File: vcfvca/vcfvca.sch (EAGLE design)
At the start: 104 parts, among them IC1 LM13700N, IC2 LM4558N, IC3 LM13700N, IC4 LM13700N, IC5 LM4558N, J1 POWER, J2 FREQ, J3 RES, J4 AMP, J5 AUD_IN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

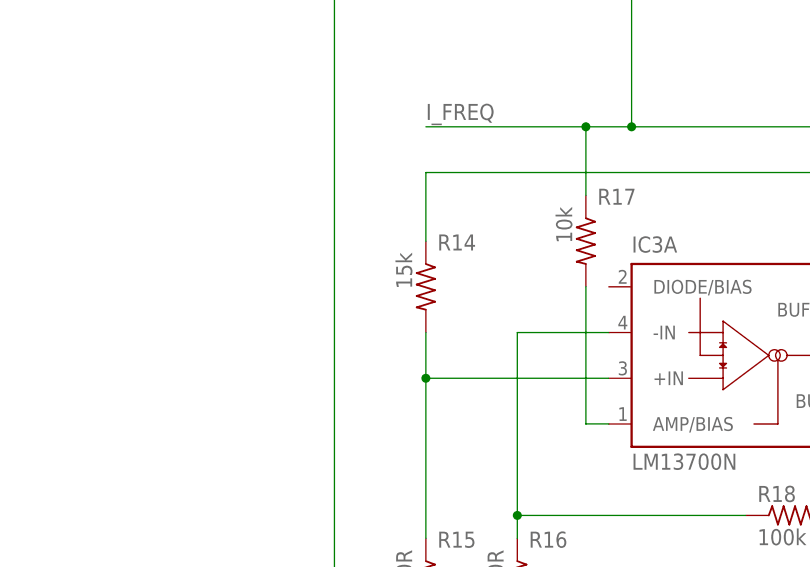
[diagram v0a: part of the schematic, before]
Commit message: Fix component value. Export to image
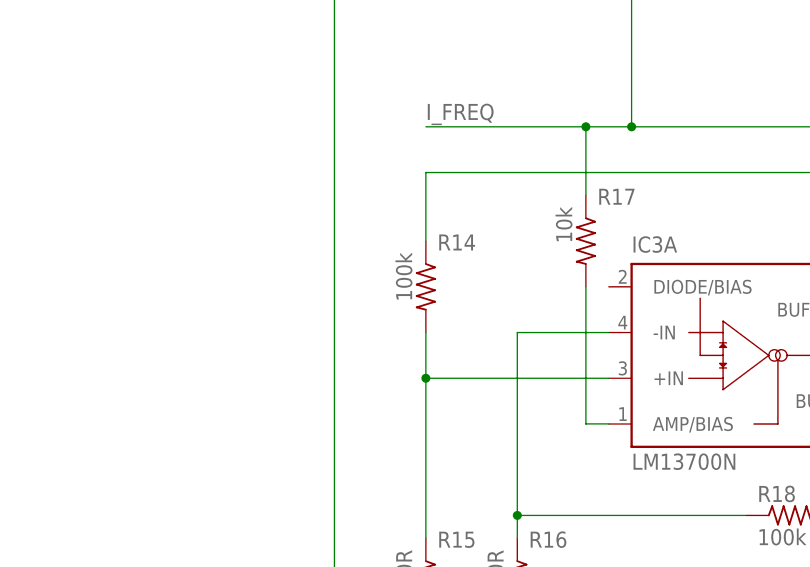
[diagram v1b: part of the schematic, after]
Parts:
- R14: value 15k -> 100k
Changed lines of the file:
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@@
 <part name="R18" library="rcl" library_urn="urn:adsk.eagle:library:334" deviceset="R-US_" device="0207/10" package3d_urn="urn:adsk.eagle:package:23491/2" value="100k"/>
 <part name="R19" library="rcl" library_urn="urn:adsk.eagle:library:334" deviceset="R-US_" device="0207/10" package3d_urn="urn:adsk.eagle:package:23491/2" value="15k"/>
-<part name="R14" library="rcl" library_urn="urn:adsk.eagle:library:334" deviceset="R-US_" device="0207/10" package3d_urn="urn:adsk.eagle:package:23491/2" value="15k"/>
+<part name="R14" library="rcl" library_urn="urn:adsk.eagle:library:334" deviceset="R-US_" device="0207/10" package3d_urn="urn:adsk.eagle:package:23491/2" value="100k"/>
 <part name="SUPPLY8" library="supply2" library_urn="urn:adsk.eagle:library:372" deviceset="+15V" device=""/>
 <part name="GND10" library="supply1" library_urn="urn:adsk.eagle:library:371" deviceset="GND" device=""/>

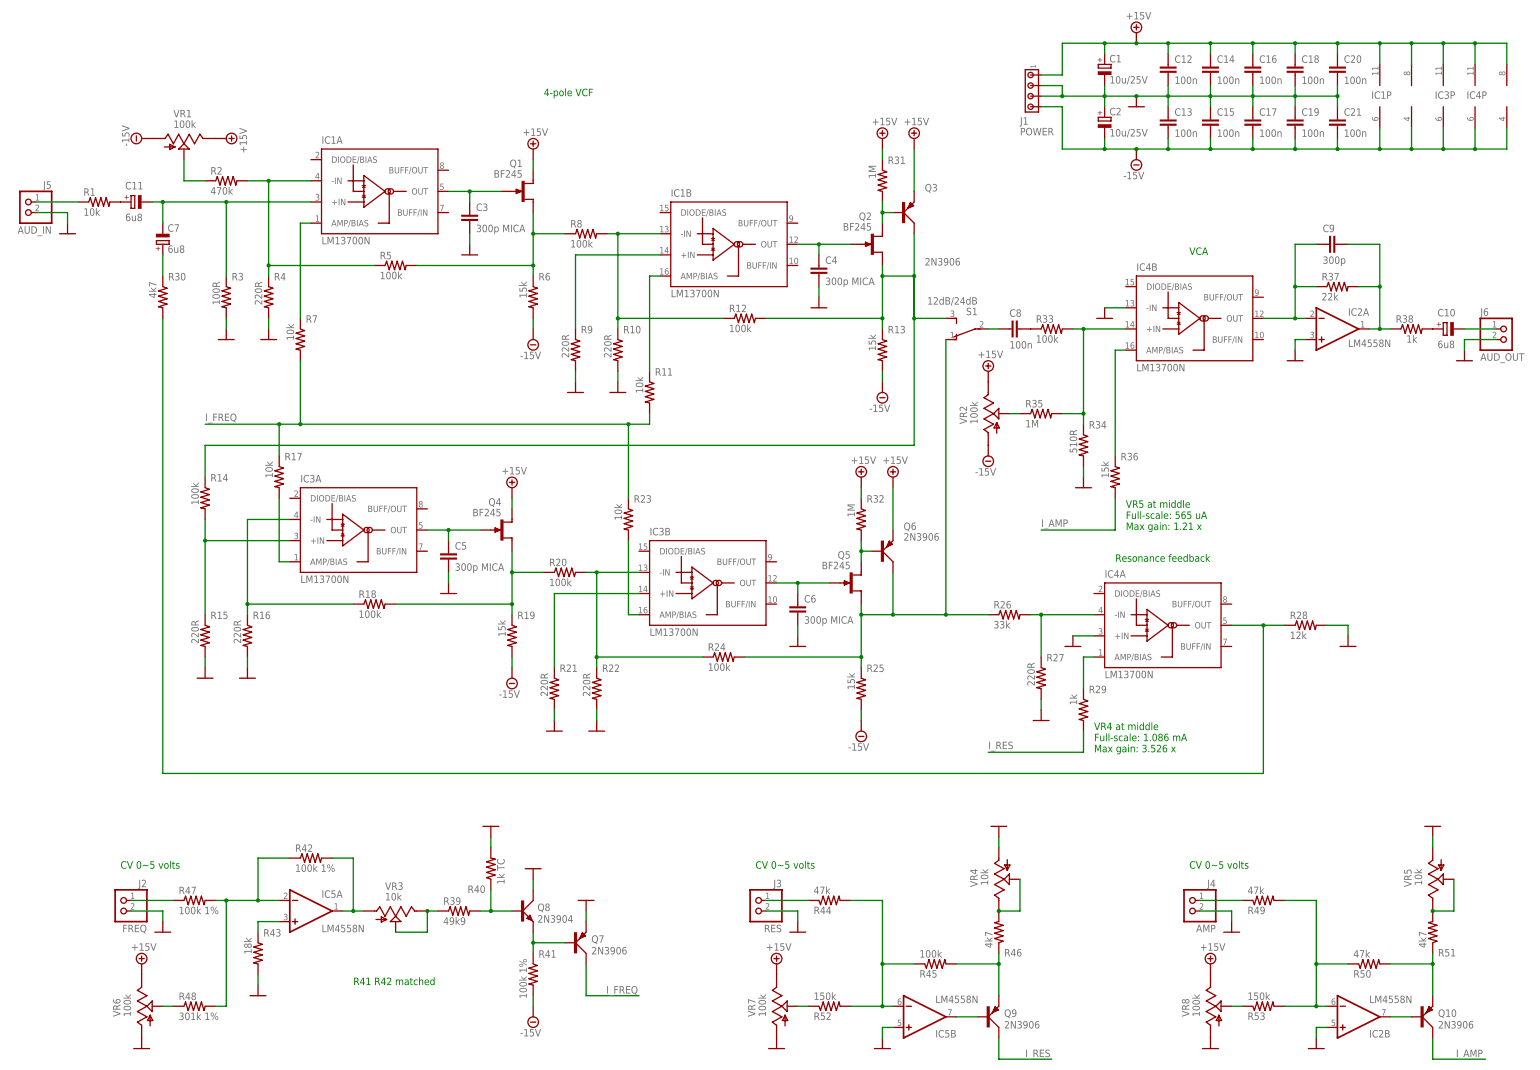
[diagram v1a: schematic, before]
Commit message: Start board placement
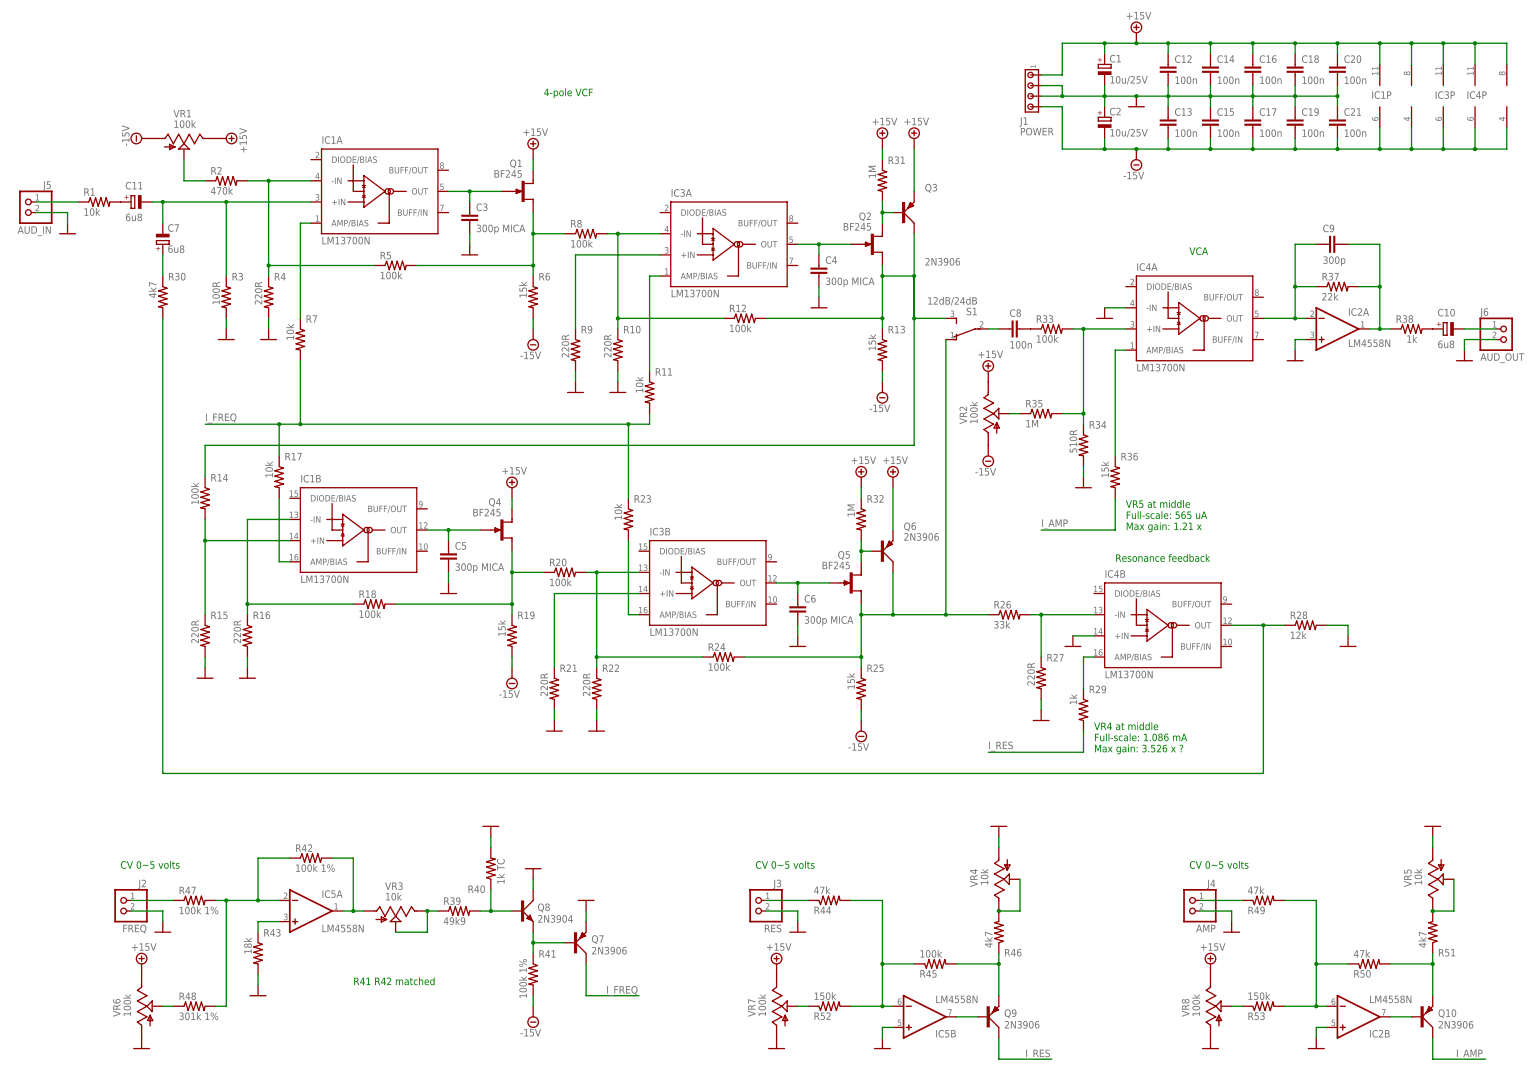
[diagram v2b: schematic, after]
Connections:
- net GND: now also IC4A.-IN, IC4B.+IN; no longer IC4A.+IN, IC4B.-IN
- net N$10: now also IC3A.AMP/BIAS; no longer IC1B.AMP/BIAS
- net N$11: now also IC3A.+IN; no longer IC1B.+IN
- net N$12: now also IC3A.-IN; no longer IC1B.-IN
- net N$14: now also IC1B.+IN; no longer IC3A.+IN
- net N$15: now also IC1B.-IN; no longer IC3A.-IN
- net N$16: now also IC4B.-IN; no longer IC4A.-IN
- net N$2: now also IC3A.OUT; no longer IC1B.OUT
- net N$22: now also IC4B.AMP/BIAS; no longer IC4A.AMP/BIAS
- net N$23: now also IC1B.AMP/BIAS; no longer IC3A.AMP/BIAS
- net N$25: now also IC4B.OUT; no longer IC4A.OUT
- net N$30: now also IC4A.+IN; no longer IC4B.+IN
- net N$31: now also IC4A.OUT; no longer IC4B.OUT
- net N$33: now also IC4A.AMP/BIAS; no longer IC4B.AMP/BIAS
- net N$4: now also IC1B.OUT; no longer IC3A.OUT
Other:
- note added: "VR4 at middle Full-scale: 1.086 mA Max gain: 3.526 x ?"
- note removed: "VR4 at middle Full-scale: 1.086 mA Max gain: 3.526 x"
- moved on the sheet: IC1B, IC3A, IC4A, IC4B
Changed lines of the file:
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@@
 <text x="261.62" y="78.74" size="1.778" layer="91">VR4 at middle
 Full-scale: 1.086 mA
-Max gain: 3.526 x</text>
+Max gain: 3.526 x ?</text>
 <text x="129.54" y="236.22" size="1.778" layer="91">4-pole VCF</text>
 <text x="284.48" y="198.12" size="1.778" layer="91">VCA</text>
@@
 <attribute name="NAME" x="328.168" y="235.585" size="1.778" layer="95"/>
 </instance>
-<instance part="IC1" gate="B" x="172.72" y="200.66" smashed="yes">
+<instance part="IC3" gate="A" x="172.72" y="200.66" smashed="yes">
 <attribute name="NAME" x="160.02" y="212.09" size="1.778" layer="95"/>
 <attribute name="VALUE" x="160.02" y="187.96" size="1.778" layer="96"/>
@@
 </instance>
 <instance part="IC2" gate="P" x="337.82" y="236.22" smashed="yes"/>
-<instance part="IC3" gate="A" x="83.82" y="132.08" smashed="yes">
+<instance part="IC1" gate="B" x="83.82" y="132.08" smashed="yes">
 <attribute name="NAME" x="71.12" y="143.51" size="1.778" layer="95"/>
 <attribute name="VALUE" x="71.12" y="119.38" size="1.778" layer="96"/>
@@
 <attribute name="VALUE" x="233.68" y="187.96" size="1.778" layer="96" rot="R180"/>
 </instance>
-<instance part="IC4" gate="B" x="284.48" y="182.88" smashed="yes">
+<instance part="IC4" gate="A" x="284.48" y="182.88" smashed="yes">
 <attribute name="NAME" x="271.78" y="194.31" size="1.778" layer="95"/>
 <attribute name="VALUE" x="271.78" y="170.18" size="1.778" layer="96"/>
@@
 <attribute name="NAME" x="351.028" y="235.585" size="1.778" layer="95"/>
 </instance>
-<instance part="IC4" gate="A" x="276.86" y="109.22" smashed="yes">
+<instance part="IC4" gate="B" x="276.86" y="109.22" smashed="yes">
 <attribute name="NAME" x="264.16" y="120.65" size="1.778" layer="95"/>
 <attribute name="VALUE" x="264.16" y="96.52" size="1.778" layer="96"/>
@@
 </segment>
 <segment>
-<pinref part="IC4" gate="A" pin="+IN"/>
+<pinref part="IC4" gate="B" pin="+IN"/>
 <pinref part="GND16" gate="1" pin="GND"/>
 <wire x1="261.62" y1="106.68" x2="256.54" y2="106.68" width="0.1524" layer="91"/>
@@
 <segment>
 <pinref part="GND18" gate="1" pin="GND"/>
-<pinref part="IC4" gate="B" pin="-IN"/>
+<pinref part="IC4" gate="A" pin="-IN"/>
 <wire x1="264.16" y1="185.42" x2="269.24" y2="185.42" width="0.1524" layer="91"/>
 </segment>
@@
 <net name="N$2" class="0">
 <segment>
-<pinref part="IC1" gate="B" pin="OUT"/>
+<pinref part="IC3" gate="A" pin="OUT"/>
 <pinref part="Q2" gate="1" pin="G"/>
 <wire x1="190.5" y1="200.66" x2="195.58" y2="200.66" width="0.1524" layer="91"/>
@@
 <net name="N$4" class="0">
 <segment>
-<pinref part="IC3" gate="A" pin="OUT"/>
+<pinref part="IC1" gate="B" pin="OUT"/>
 <pinref part="Q4" gate="1" pin="G"/>
 <wire x1="101.6" y1="132.08" x2="106.68" y2="132.08" width="0.1524" layer="91"/>
@@
 <pinref part="R11" gate="G$1" pin="1"/>
 <wire x1="154.94" y1="170.18" x2="154.94" y2="193.04" width="0.1524" layer="91"/>
-<pinref part="IC1" gate="B" pin="AMP/BIAS"/>
+<pinref part="IC3" gate="A" pin="AMP/BIAS"/>
 <wire x1="154.94" y1="193.04" x2="157.48" y2="193.04" width="0.1524" layer="91"/>
 </segment>
@@
 <segment>
 <pinref part="R8" gate="G$1" pin="2"/>
-<pinref part="IC1" gate="B" pin="-IN"/>
+<pinref part="IC3" gate="A" pin="-IN"/>
 <wire x1="144.78" y1="203.2" x2="147.32" y2="203.2" width="0.1524" layer="91"/>
 <pinref part="R10" gate="G$1" pin="1"/>
@@
 <net name="N$11" class="0">
 <segment>
-<pinref part="IC1" gate="B" pin="+IN"/>
+<pinref part="IC3" gate="A" pin="+IN"/>
 <wire x1="157.48" y1="198.12" x2="137.16" y2="198.12" width="0.1524" layer="91"/>
 <pinref part="R9" gate="G$1" pin="1"/>
@@
 <net name="N$14" class="0">
 <segment>
-<pinref part="IC3" gate="A" pin="+IN"/>
+<pinref part="IC1" gate="B" pin="+IN"/>
 <wire x1="68.58" y1="129.54" x2="48.26" y2="129.54" width="0.1524" layer="91"/>
 <pinref part="R15" gate="G$1" pin="1"/>
@@
 <pinref part="R16" gate="G$1" pin="1"/>
 <wire x1="58.42" y1="111.76" x2="58.42" y2="114.3" width="0.1524" layer="91"/>
-<pinref part="IC3" gate="A" pin="-IN"/>
+<pinref part="IC1" gate="B" pin="-IN"/>
 <wire x1="58.42" y1="114.3" x2="58.42" y2="134.62" width="0.1524" layer="91"/>
 <wire x1="58.42" y1="134.62" x2="68.58" y2="134.62" width="0.1524" layer="91"/>
@@
 <segment>
 <pinref part="R17" gate="G$1" pin="2"/>
-<pinref part="IC3" gate="A" pin="AMP/BIAS"/>
+<pinref part="IC1" gate="B" pin="AMP/BIAS"/>
 <wire x1="68.58" y1="124.46" x2="66.04" y2="124.46" width="0.1524" layer="91"/>
 <wire x1="66.04" y1="139.7" x2="66.04" y2="124.46" width="0.1524" layer="91"/>
@@
 <net name="N$16" class="0">
 <segment>
-<pinref part="IC4" gate="A" pin="-IN"/>
+<pinref part="IC4" gate="B" pin="-IN"/>
 <pinref part="R26" gate="G$1" pin="2"/>
 <wire x1="261.62" y1="111.76" x2="248.92" y2="111.76" width="0.1524" layer="91"/>
@@
 <net name="N$22" class="0">
 <segment>
-<pinref part="IC4" gate="A" pin="AMP/BIAS"/>
+<pinref part="IC4" gate="B" pin="AMP/BIAS"/>
 <wire x1="261.62" y1="101.6" x2="259.08" y2="101.6" width="0.1524" layer="91"/>
 <pinref part="R29" gate="G$1" pin="1"/>
@@
 <net name="N$25" class="0">
 <segment>
-<pinref part="IC4" gate="A" pin="OUT"/>
+<pinref part="IC4" gate="B" pin="OUT"/>
 <wire x1="294.64" y1="109.22" x2="302.26" y2="109.22" width="0.1524" layer="91"/>
 <wire x1="302.26" y1="109.22" x2="302.26" y2="73.66" width="0.1524" layer="91"/>
@@
 <net name="N$30" class="0">
 <segment>
-<pinref part="IC4" gate="B" pin="+IN"/>
+<pinref part="IC4" gate="A" pin="+IN"/>
 <pinref part="R33" gate="G$1" pin="2"/>
 <wire x1="269.24" y1="180.34" x2="259.08" y2="180.34" width="0.1524" layer="91"/>
@@
 <net name="N$33" class="0">
 <segment>
-<pinref part="IC4" gate="B" pin="AMP/BIAS"/>
+<pinref part="IC4" gate="A" pin="AMP/BIAS"/>
 <wire x1="269.24" y1="175.26" x2="266.7" y2="175.26" width="0.1524" layer="91"/>
 <pinref part="R36" gate="G$1" pin="1"/>
@@
 <net name="N$31" class="0">
 <segment>
-<pinref part="IC4" gate="B" pin="OUT"/>
+<pinref part="IC4" gate="A" pin="OUT"/>
 <wire x1="309.88" y1="182.88" x2="302.26" y2="182.88" width="0.1524" layer="91"/>
 <pinref part="IC2" gate="A" pin="-IN"/>

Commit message: Done placement
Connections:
- net GND: now also IC4A.+IN, IC4B.-IN; no longer IC4A.-IN, IC4B.+IN
- net N$16: now also IC4A.-IN; no longer IC4B.-IN
- net N$22: now also IC4A.AMP/BIAS; no longer IC4B.AMP/BIAS
- net N$25: now also IC4A.OUT; no longer IC4B.OUT
- net N$30: now also IC4B.+IN; no longer IC4A.+IN
- net N$31: now also IC2B.-IN, IC4B.OUT; no longer IC2A.-IN, IC4A.OUT
- net N$33: now also IC4B.AMP/BIAS; no longer IC4A.AMP/BIAS
- net N$35: now also IC2B.OUT; no longer IC2A.OUT
- net N$50: now also IC2A.OUT; no longer IC2B.OUT
- net N$52: now also IC2A.-IN; no longer IC2B.-IN
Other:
- moved on the sheet: IC2A, IC2B, IC4A, IC4B
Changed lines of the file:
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@@
 <attribute name="VALUE" x="220.98" y="195.58" size="1.778" layer="96"/>
 </instance>
-<instance part="IC2" gate="A" x="320.04" y="180.34" smashed="yes" rot="MR180">
+<instance part="IC2" gate="B" x="320.04" y="180.34" smashed="yes" rot="MR180">
 <attribute name="NAME" x="322.58" y="183.515" size="1.778" layer="95"/>
 <attribute name="VALUE" x="322.58" y="176.022" size="1.778" layer="96"/>
 </instance>
-<instance part="IC2" gate="B" x="325.12" y="15.24" smashed="yes" rot="MR180">
+<instance part="IC2" gate="A" x="325.12" y="15.24" smashed="yes" rot="MR180">
 <attribute name="NAME" x="327.66" y="12.065" size="1.778" layer="95" rot="MR180"/>
 <attribute name="VALUE" x="327.66" y="20.32" size="1.778" layer="96" rot="MR180"/>
@@
 <attribute name="VALUE" x="233.68" y="187.96" size="1.778" layer="96" rot="R180"/>
 </instance>
-<instance part="IC4" gate="A" x="284.48" y="182.88" smashed="yes">
+<instance part="IC4" gate="B" x="284.48" y="182.88" smashed="yes">
 <attribute name="NAME" x="271.78" y="194.31" size="1.778" layer="95"/>
 <attribute name="VALUE" x="271.78" y="170.18" size="1.778" layer="96"/>
@@
 <attribute name="NAME" x="351.028" y="235.585" size="1.778" layer="95"/>
 </instance>
-<instance part="IC4" gate="B" x="276.86" y="109.22" smashed="yes">
+<instance part="IC4" gate="A" x="276.86" y="109.22" smashed="yes">
 <attribute name="NAME" x="264.16" y="120.65" size="1.778" layer="95"/>
 <attribute name="VALUE" x="264.16" y="96.52" size="1.778" layer="96"/>
@@
 </segment>
 <segment>
-<pinref part="IC4" gate="B" pin="+IN"/>
+<pinref part="IC4" gate="A" pin="+IN"/>
 <pinref part="GND16" gate="1" pin="GND"/>
 <wire x1="261.62" y1="106.68" x2="256.54" y2="106.68" width="0.1524" layer="91"/>
@@
 <segment>
 <pinref part="GND18" gate="1" pin="GND"/>
-<pinref part="IC4" gate="A" pin="-IN"/>
+<pinref part="IC4" gate="B" pin="-IN"/>
 <wire x1="264.16" y1="185.42" x2="269.24" y2="185.42" width="0.1524" layer="91"/>
 </segment>
 <segment>
-<pinref part="IC2" gate="A" pin="+IN"/>
+<pinref part="IC2" gate="B" pin="+IN"/>
 <pinref part="GND19" gate="1" pin="GND"/>
 <wire x1="312.42" y1="177.8" x2="309.88" y2="177.8" width="0.1524" layer="91"/>
@@
 </segment>
 <segment>
-<pinref part="IC2" gate="B" pin="+IN"/>
+<pinref part="IC2" gate="A" pin="+IN"/>
 <wire x1="317.5" y1="12.7" x2="314.96" y2="12.7" width="0.1524" layer="91"/>
 <pinref part="GND27" gate="1" pin="GND"/>
@@
 <net name="N$16" class="0">
 <segment>
-<pinref part="IC4" gate="B" pin="-IN"/>
+<pinref part="IC4" gate="A" pin="-IN"/>
 <pinref part="R26" gate="G$1" pin="2"/>
 <wire x1="261.62" y1="111.76" x2="248.92" y2="111.76" width="0.1524" layer="91"/>
@@
 <net name="N$22" class="0">
 <segment>
-<pinref part="IC4" gate="B" pin="AMP/BIAS"/>
+<pinref part="IC4" gate="A" pin="AMP/BIAS"/>
 <wire x1="261.62" y1="101.6" x2="259.08" y2="101.6" width="0.1524" layer="91"/>
 <pinref part="R29" gate="G$1" pin="1"/>
@@
 <net name="N$25" class="0">
 <segment>
-<pinref part="IC4" gate="B" pin="OUT"/>
+<pinref part="IC4" gate="A" pin="OUT"/>
 <wire x1="294.64" y1="109.22" x2="302.26" y2="109.22" width="0.1524" layer="91"/>
 <wire x1="302.26" y1="109.22" x2="302.26" y2="73.66" width="0.1524" layer="91"/>
@@
 <net name="N$30" class="0">
 <segment>
-<pinref part="IC4" gate="A" pin="+IN"/>
+<pinref part="IC4" gate="B" pin="+IN"/>
 <pinref part="R33" gate="G$1" pin="2"/>
 <wire x1="269.24" y1="180.34" x2="259.08" y2="180.34" width="0.1524" layer="91"/>
@@
 <net name="N$33" class="0">
 <segment>
-<pinref part="IC4" gate="A" pin="AMP/BIAS"/>
+<pinref part="IC4" gate="B" pin="AMP/BIAS"/>
 <wire x1="269.24" y1="175.26" x2="266.7" y2="175.26" width="0.1524" layer="91"/>
 <pinref part="R36" gate="G$1" pin="1"/>
@@
 <wire x1="325.12" y1="190.5" x2="330.2" y2="190.5" width="0.1524" layer="91"/>
 <junction x="330.2" y="190.5"/>
-<pinref part="IC2" gate="A" pin="OUT"/>
+<pinref part="IC2" gate="B" pin="OUT"/>
 <wire x1="327.66" y1="180.34" x2="330.2" y2="180.34" width="0.1524" layer="91"/>
 <junction x="330.2" y="180.34"/>
@@
 <segment>
 <pinref part="Q10" gate="1" pin="B"/>
-<pinref part="IC2" gate="B" pin="OUT"/>
+<pinref part="IC2" gate="A" pin="OUT"/>
 <wire x1="337.82" y1="15.24" x2="332.74" y2="15.24" width="0.1524" layer="91"/>
 </segment>
@@
 <net name="N$52" class="0">
 <segment>
-<pinref part="IC2" gate="B" pin="-IN"/>
+<pinref part="IC2" gate="A" pin="-IN"/>
 <pinref part="R50" gate="G$1" pin="1"/>
 <wire x1="314.96" y1="17.78" x2="317.5" y2="17.78" width="0.1524" layer="91"/>
@@
 <net name="N$31" class="0">
 <segment>
-<pinref part="IC4" gate="A" pin="OUT"/>
+<pinref part="IC4" gate="B" pin="OUT"/>
 <wire x1="309.88" y1="182.88" x2="302.26" y2="182.88" width="0.1524" layer="91"/>
-<pinref part="IC2" gate="A" pin="-IN"/>
+<pinref part="IC2" gate="B" pin="-IN"/>
 <wire x1="309.88" y1="182.88" x2="312.42" y2="182.88" width="0.1524" layer="91"/>
 <pinref part="R37" gate="G$1" pin="1"/>
